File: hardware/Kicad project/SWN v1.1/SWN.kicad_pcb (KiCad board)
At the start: 2 copper layers, 130.6 x 112 mm, 627 parts, among them IC10 LD1117ADT33TR, IC11 TLV171, IC12 TL082, IC13 TL082, IC2 NJM2068, IC3 NJM2068, IC4 NJM2068, IC5 NJM2068, IC6 TL082, IC7 MCP1703x-3302E/MB, IC8 TL082, IC9 TL082, J1 HEADER-1X3-TH, J2 HEADER-2X8-TH, J3 Conn_02x04_Odd_Even, SW1 submini-3T, SW2 submini-2T, U1 WM8731, U10 PCA9685, U11 PCA9685, U12 PCA9685, U13 PCA9685, U14 TLV171, U15 ADS8634, U16 TLV171, U17 ADS8634, U18 TLV171, U19 TLV171, U2 PCA9685, U20 TLV171, U21 TLV171, U23 MCP1703x-3302E/MB, U24 TLV171, U3 PCA9685, U4 PCA9685, U5 PCA9685, U6 PCA9685, U7 STM32F765ZG, U8 S25FL127, U9 PCA9685, X1 16MHz

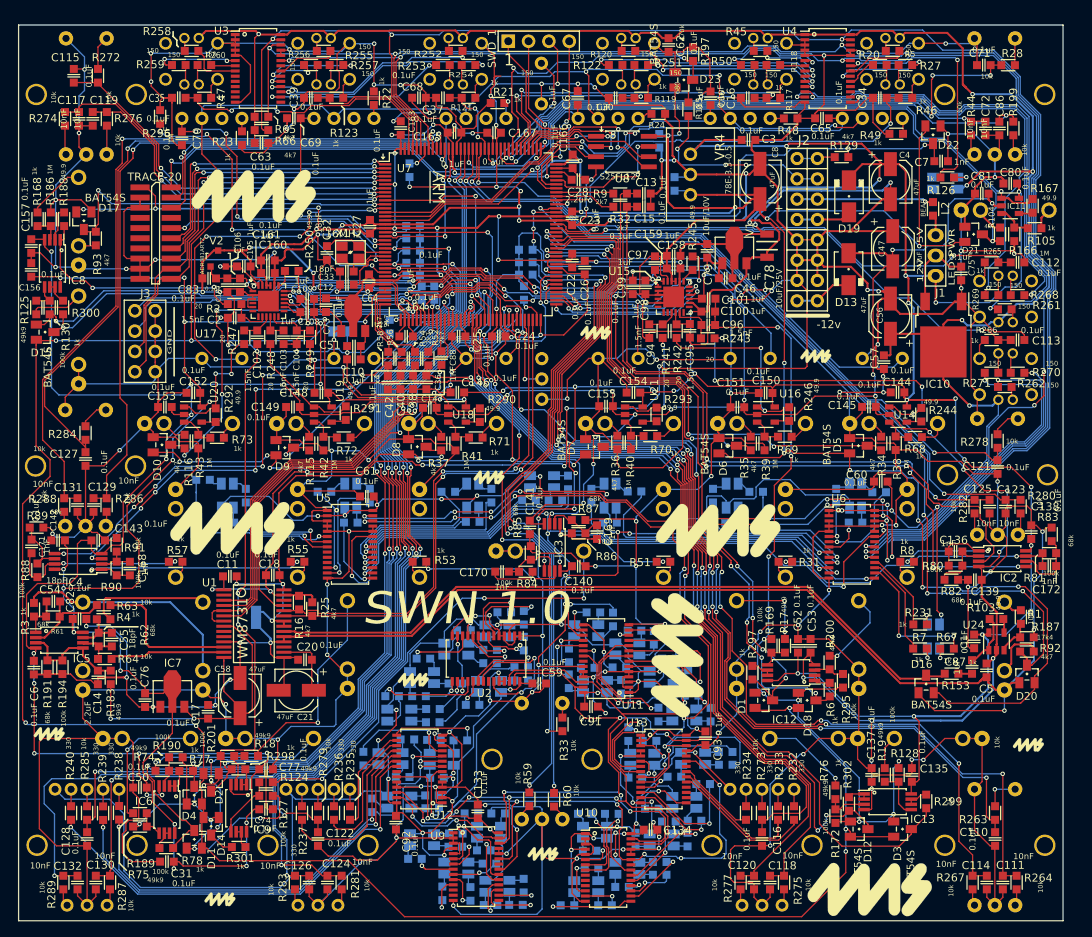
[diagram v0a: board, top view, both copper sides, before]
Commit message: Updated LICENSE, README, and removed 4ms logos from PCB
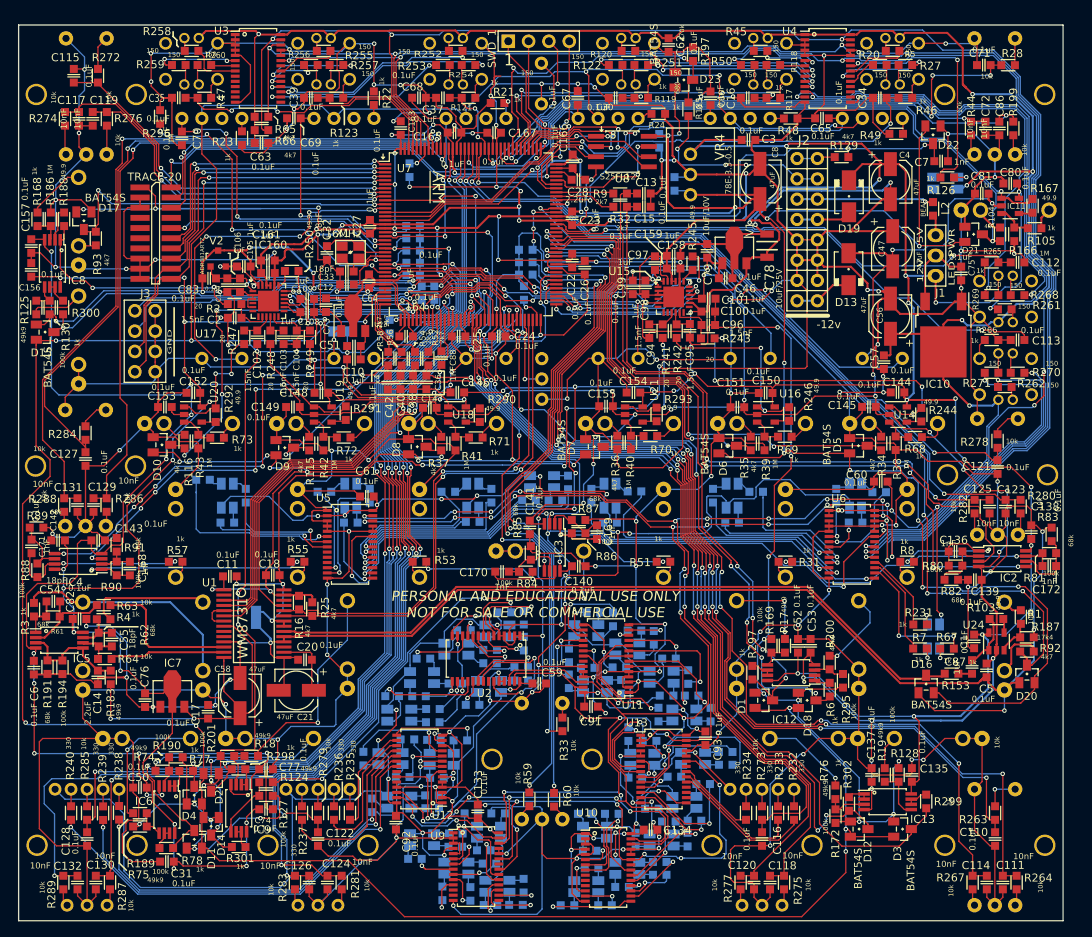
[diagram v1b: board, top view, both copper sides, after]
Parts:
- removed G***1, G***2, G***3, G***4, G***5: 4ms-logo, 4ms_Symbol:4msLogo_15.5x6.6mm
- removed G***10, G***11, G***12, G***13, G***6, G***7, G***8, G***9: 4ms-logo, 4ms_Symbol:4msLogo_3.8x1.7mm
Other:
- board text added: "PERSONAL AND EDUCATIONAL USE ONLY NOT FOR SALE OR COMMERCIAL USE"
- board text removed: "SWN 1.0"
